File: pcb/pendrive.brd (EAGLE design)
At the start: 100 x 80 mm, 22 parts, among them IC1 MCP1703CB, U1 F55[0/1]X---RGZ48, U2 MICROSD-MOLEX, X1 USBPCB, Y1 RESONATORSMD

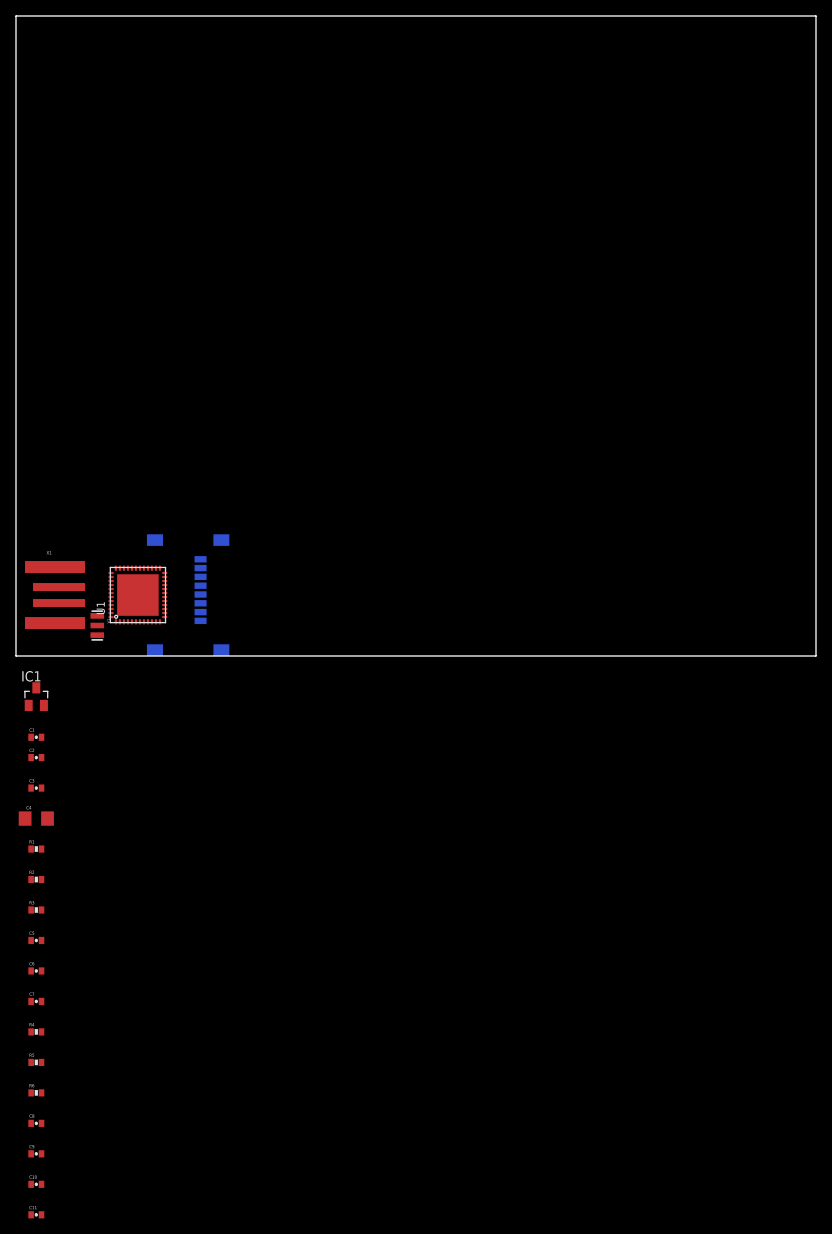
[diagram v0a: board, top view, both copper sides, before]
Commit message: First layout of components, not routed yet
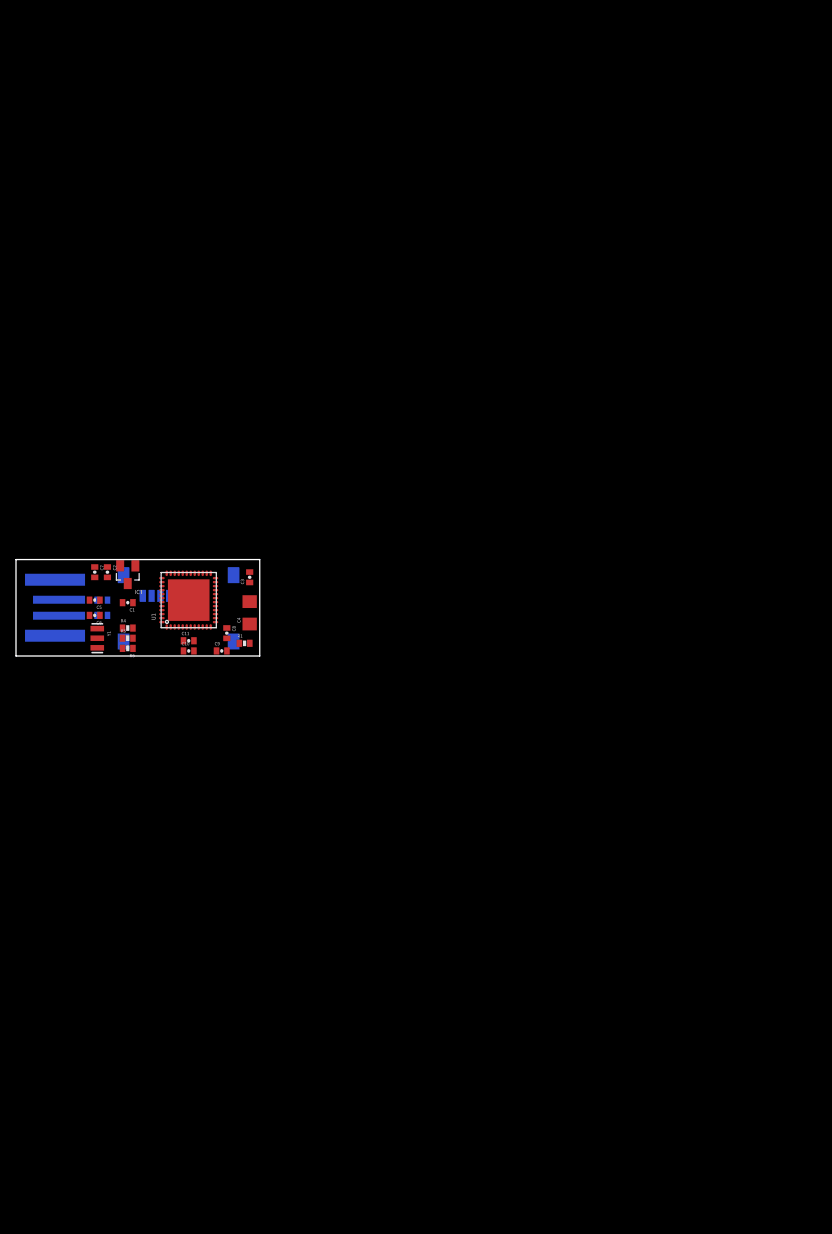
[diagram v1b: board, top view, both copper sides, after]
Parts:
- moved C11 74.2 mm to (21.6, 1.91)
- moved C10 69.3 mm to (21.6, 0.64)
- moved C9 67.0 mm to (25.7, 0.64)
- moved C8 65.7 mm to (26.4, 2.86), turned to 270 degrees
- moved R6 56.7 mm to (14.0, 0.95), turned to 180 degrees
- moved R5 54.2 mm to (14.0, 2.22)
- moved C7 54.2 mm to (9.84, 10.5), turned to 270 degrees
- moved R4 51.8 mm to (14.0, 3.49)
- moved C6 45.0 mm to (9.84, 5.08), turned to 180 degrees
- moved C5 43.2 mm to (9.84, 6.99), turned to 180 degrees
- moved R3 39.6 mm to (10.8, 6.99), flipped to the bottom, turned to 180 degrees
- moved C3 37.5 mm to (29.2, 9.84), turned to 90 degrees
- moved C4 37.0 mm to (29.2, 5.40), turned to 90 degrees
- moved R1 36.6 mm to (28.6, 1.59)
- moved R2 34.0 mm to (10.8, 5.08), flipped to the bottom, turned to 180 degrees
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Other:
- board size 100 x 80 mm -> 30.5 x 12.1 mm

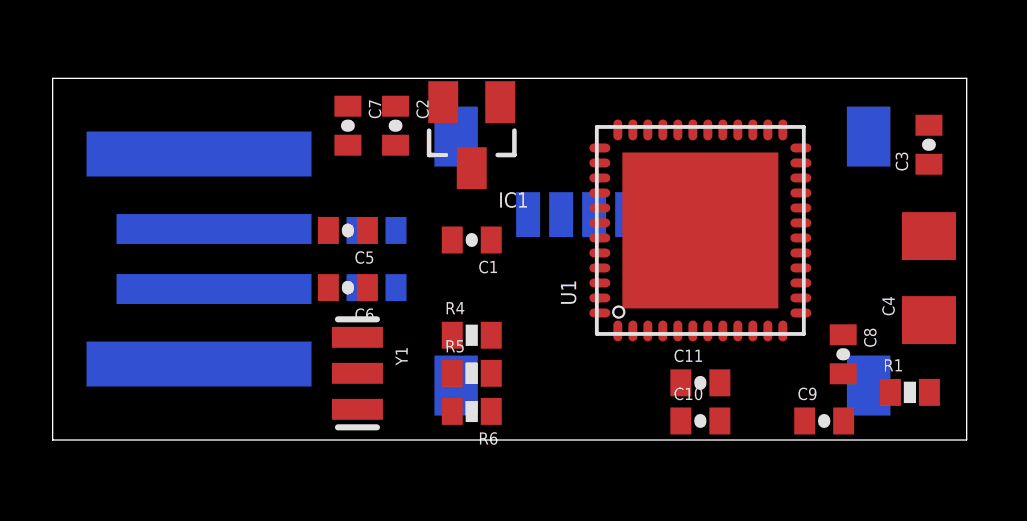
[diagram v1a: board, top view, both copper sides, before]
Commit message: Added first routed PCB version, not tested yet
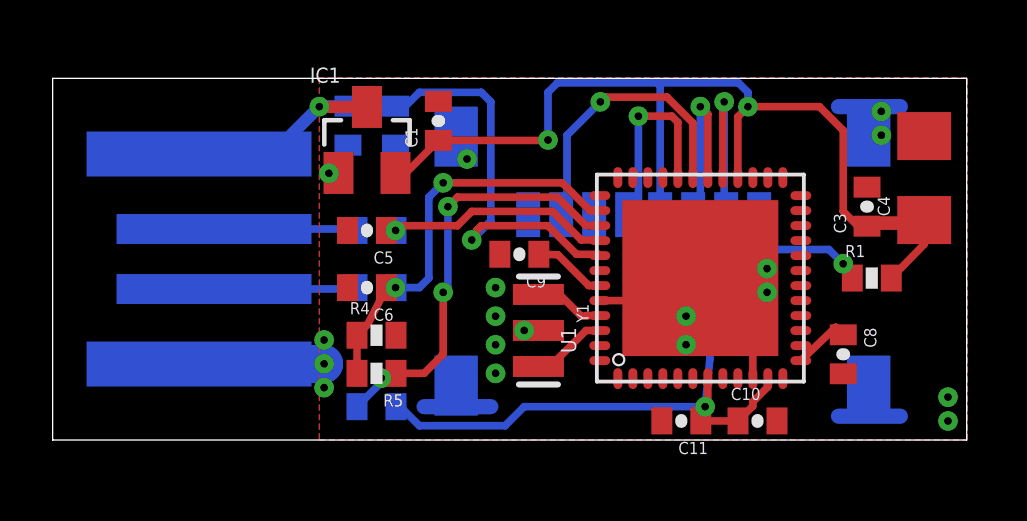
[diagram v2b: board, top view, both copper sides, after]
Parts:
- moved C9 11.6 mm to (15.6, 6.19), turned to 180 degrees
- moved Y1 6.20 mm to (16.2, 3.65)
- moved C1 4.12 mm to (12.9, 10.6), turned to 90 degrees
- moved R1 4.02 mm to (27.3, 5.40)
- moved IC1 3.50 mm to (10.5, 10.0), turned to 0 degrees
- moved C4 3.34 mm to (29.1, 8.73)
- moved R6 3.18 mm to (10.8, 1.11), flipped to the bottom, turned to 0 degrees
- moved R4 3.18 mm to (10.8, 3.49)
- moved R5 3.18 mm to (10.8, 2.22), turned to 180 degrees
- moved C3 2.92 mm to (27.1, 7.78)
- moved C10 1.91 mm to (23.5, 0.64)
- moved U1 1.59 mm to (21.6, 5.40)
- moved C11 1.42 mm to (21.0, 0.64), turned to 180 degrees
- moved C5 0.63 mm to (10.5, 6.99)
- moved C6 0.63 mm to (10.5, 5.08)
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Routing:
- net 3.3V: track 0.00 -> 57.5 mm, vias 0 -> 3
- net 5V: track 0.00 -> 22.2 mm, vias 0 -> 2
- net GND: track 0.00 -> 20.4 mm, vias 0 -> 18
- net PUR: track 0.00 -> 14.3 mm, vias 0 -> 3
- net USB_DP: track 0.00 -> 13.7 mm, vias 0 -> 2
- net SD_CS: track 0.00 -> 12.0 mm, vias 0 -> 2
- net SOMI: track 0.00 -> 9.63 mm, vias 0 -> 1
- net USB_DM: track 0.00 -> 7.81 mm, vias 0 -> 1
- net CLK: track 0.00 -> 6.68 mm, vias 0 -> 1
- net SIMO: track 0.00 -> 6.17 mm, vias 0 -> 1
- net N$2: track 0.00 -> 4.78 mm
- net N$1: track 0.00 -> 4.78 mm
- net N$5: track 0.00 -> 2.55 mm
- net 1.8V: track 0.00 -> 2.46 mm
- net N$4: track 0.00 -> 2.41 mm
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- added copper zone on layer 1, net GND
- added copper zone on layer 16, net GND

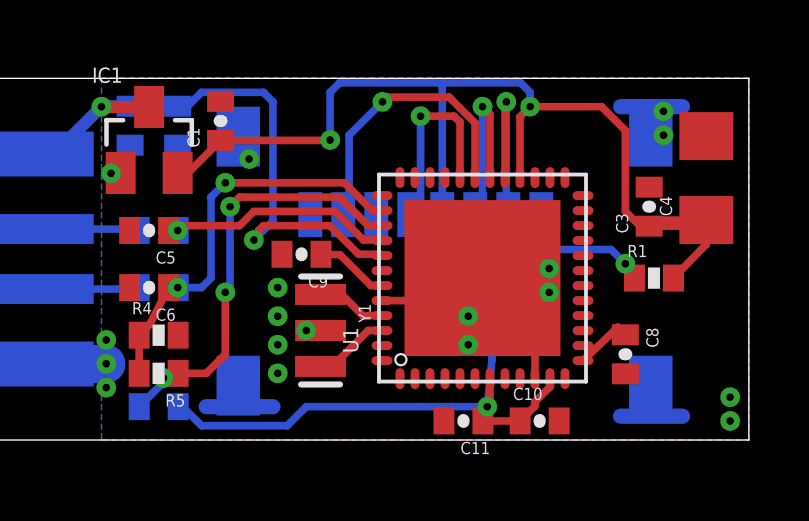
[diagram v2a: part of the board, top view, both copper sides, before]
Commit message: Added programming and test points
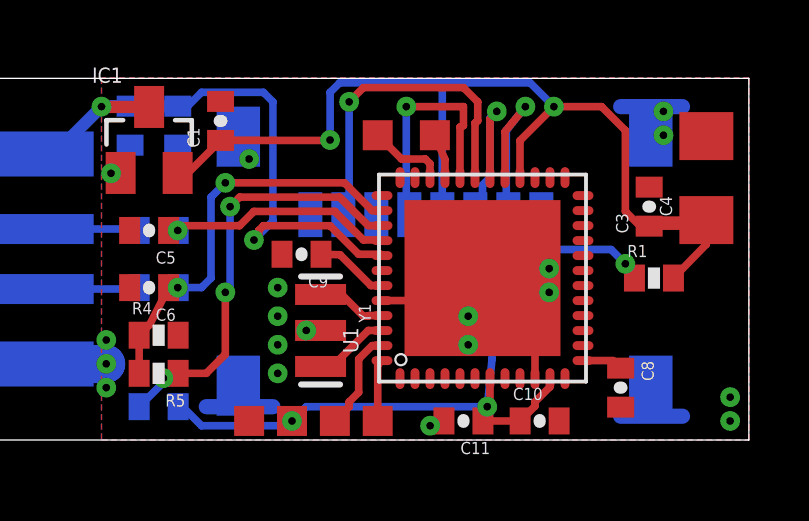
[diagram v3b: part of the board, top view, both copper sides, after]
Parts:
- added TP1, TP2, TP3, TP4, TP5, TP6: PTR1TP10SQ, testpad:TP10SQ
- moved C8 1.12 mm to (26.2, 1.75)
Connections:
- net 3.3V: now also TP3.TP
- net DEBUG_RXD: now also TP5.TP
- net DEBUG_TXD: now also TP6.TP
- net GND: now also TP4.TP
- net RST: now also TP1.TP
- net TEST: now also TP2.TP
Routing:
- net TEST: track 0.00 -> 3.36 mm
- net DEBUG_RXD: track 0.00 -> 2.60 mm
- net RST: track 0.00 -> 2.07 mm
- net DEBUG_TXD: track 0.00 -> 1.48 mm
- net SOMI: track 9.63 -> 11.1 mm
- net CLK: track 6.68 -> 7.96 mm
- net GND: track 20.4 -> 21.5 mm, vias 18 -> 19
- net VCORE: track 1.96 -> 1.36 mm
- net 3.3V: track 57.5 -> 57.6 mm, vias 3 -> 4

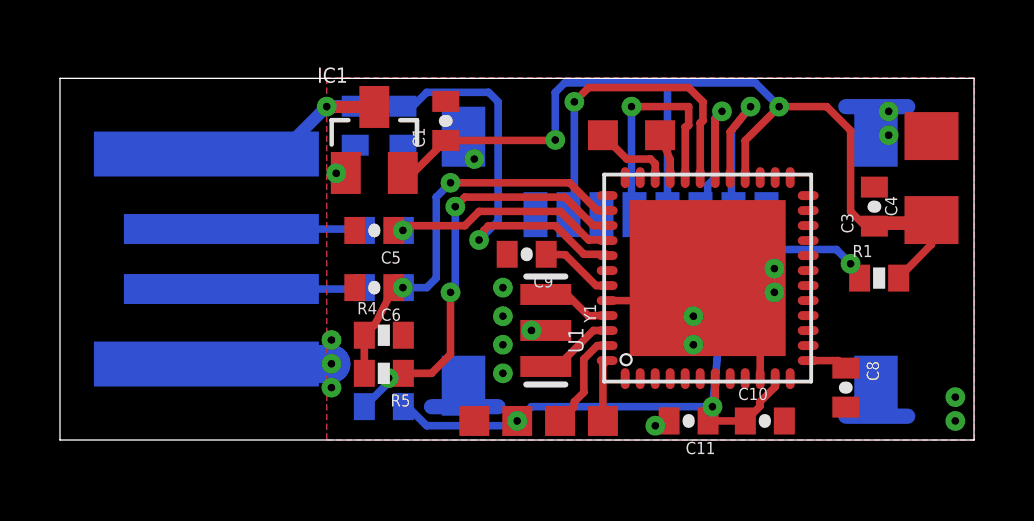
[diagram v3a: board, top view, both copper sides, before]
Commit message: Shrinked the board a little bit
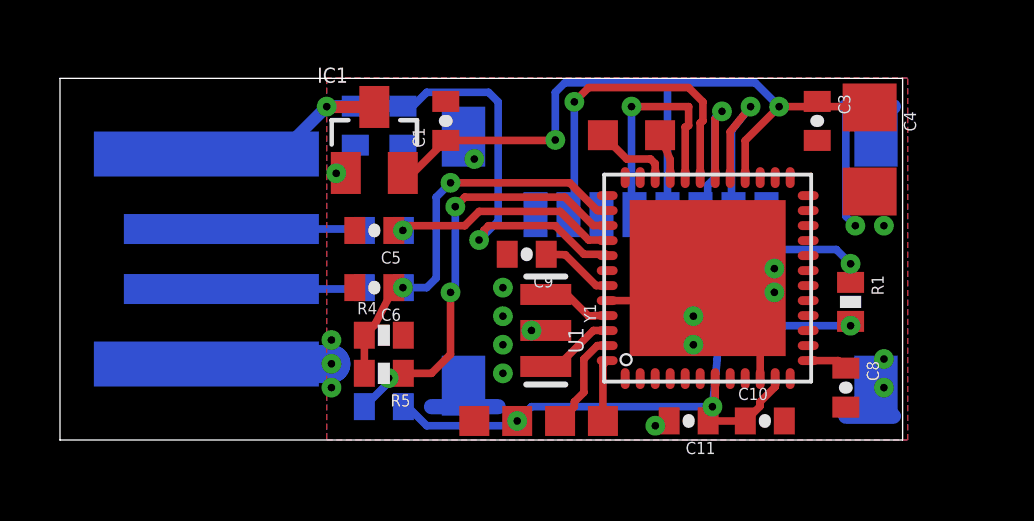
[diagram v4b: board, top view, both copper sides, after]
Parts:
- moved C3 3.43 mm to (25.2, 10.6), turned to 270 degrees
- moved C4 2.27 mm to (27.0, 9.68), turned to 270 degrees
- moved R1 1.24 mm to (26.4, 4.60), turned to 270 degrees
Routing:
- net 3.3V: track 57.6 -> 52.7 mm, vias 4 -> 5
- net GND: track 21.5 -> 25.6 mm
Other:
- board size 30.5 x 12.1 mm -> 28.1 x 12.1 mm
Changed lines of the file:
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@@
 <board>
 <plain>
-<wire x1="0" y1="0" x2="30.4675" y2="0" width="0" layer="20"/>
-<wire x1="30.4675" y1="0" x2="30.4675" y2="12.055" width="0" layer="20"/>
-<wire x1="30.4675" y1="12.055" x2="0" y2="12.055" width="0" layer="20"/>
+<wire x1="0" y1="0" x2="28.08625" y2="0" width="0" layer="20"/>
+<wire x1="28.08625" y1="0" x2="28.08625" y2="12.055" width="0" layer="20"/>
+<wire x1="28.08625" y1="12.055" x2="0" y2="12.055" width="0" layer="20"/>
 <wire x1="0" y1="12.055" x2="0" y2="0" width="0" layer="20"/>
 </plain>
@@
 <element name="C1" library="SparkFun" package="0402-CAP" value="1uF / 10V" x="12.85875" y="10.63625" rot="R90"/>
 <element name="C2" library="SparkFun" package="0402-CAP" value="1uF / 10V" x="11.43" y="10.4775" rot="MR270"/>
-<element name="C3" library="SparkFun" package="0402-CAP" value="0.1uF / 10V" x="27.14625" y="7.77875" rot="R90"/>
-<element name="C4" library="SparkFun" package="1206" value="10uF / 10V" x="29.05125" y="8.73125" rot="R90"/>
-<element name="R1" library="SparkFun" package="0402-RES" value="47k" x="27.305" y="5.3975"/>
+<element name="C3" library="SparkFun" package="0402-CAP" value="0.1uF / 10V" x="25.24125" y="10.63625" rot="R270"/>
+<element name="C4" library="SparkFun" package="1206" value="10uF / 10V" x="26.9875" y="9.68375" rot="R270"/>
+<element name="R1" library="SparkFun" package="0402-RES" value="47k" x="26.3525" y="4.60375" rot="R270"/>
 <element name="R2" library="SparkFun" package="0402-RES" value="27" x="10.795" y="5.08" rot="MR180"/>
 <element name="R3" library="SparkFun" package="0402-RES" value="27" x="10.795" y="6.985" rot="MR180"/>
@@
 <vertex x="8.89" y="12.065"/>
 <vertex x="8.89" y="0"/>
-<vertex x="30.48" y="0"/>
-<vertex x="30.48" y="12.065"/>
+<vertex x="28.2575" y="0"/>
+<vertex x="28.2575" y="12.065"/>
 </polygon>
 <polygon width="0.254" layer="1">
 <vertex x="8.89" y="12.065"/>
 <vertex x="8.89" y="0"/>
-<vertex x="30.48" y="0"/>
-<vertex x="30.48" y="12.065"/>
+<vertex x="28.2575" y="0"/>
+<vertex x="28.2575" y="12.065"/>
 </polygon>
 <via x="9.04875" y="3.33375" extent="1-16" drill="0.254"/>
@@
 <wire x1="12.3825" y1="1.11125" x2="14.605" y2="1.11125" width="0.508" layer="16"/>
 <via x="13.81125" y="9.36625" extent="1-16" drill="0.254"/>
-<wire x1="26.19375" y1="11.1125" x2="28.2575" y2="11.1125" width="0.508" layer="16"/>
-<wire x1="26.19375" y1="0.79375" x2="28.2575" y2="0.79375" width="0.508" layer="16"/>
-<via x="29.845" y="0.635" extent="1-16" drill="0.254"/>
-<via x="29.845" y="1.42875" extent="1-16" drill="0.254"/>
+<wire x1="26.19375" y1="11.1125" x2="27.78125" y2="11.1125" width="0.508" layer="16"/>
+<wire x1="26.19375" y1="0.79375" x2="27.78125" y2="0.79375" width="0.508" layer="16"/>
+<via x="27.46375" y="1.74625" extent="1-16" drill="0.254"/>
+<via x="27.46375" y="2.69875" extent="1-16" drill="0.254"/>
 <via x="21.11375" y="3.175" extent="1-16" drill="0.254"/>
 <via x="21.11375" y="4.1275" extent="1-16" drill="0.254"/>
@@
 <wire x1="18.24" y1="4.6475" x2="20.59375" y2="4.6475" width="0.254" layer="1"/>
 <wire x1="20.59375" y1="4.6475" x2="21.11375" y2="4.1275" width="0.254" layer="1"/>
-<via x="27.6225" y="10.95375" extent="1-16" drill="0.254"/>
-<via x="27.6225" y="10.16" extent="1-16" drill="0.254"/>
+<via x="26.51125" y="7.14375" extent="1-16" drill="0.254"/>
+<via x="27.46375" y="7.14375" extent="1-16" drill="0.254"/>
 <wire x1="4.88" y1="2.5325" x2="9.04125" y2="2.5325" width="1.27" layer="16"/>
 <wire x1="9.04125" y1="2.5325" x2="9.04875" y2="2.54" width="1.27" layer="16"/>
 <via x="9.2075" y="8.89" extent="1-16" drill="0.254"/>
-<wire x1="28.2575" y1="11.1125" x2="27.78125" y2="11.1125" width="0.254" layer="16"/>
-<wire x1="27.78125" y1="11.1125" x2="27.6225" y2="10.95375" width="0.254" layer="16"/>
 <wire x1="23.34" y1="2.0475" x2="23.34" y2="4.44875" width="0.254" layer="1"/>
 <wire x1="23.34" y1="4.44875" x2="23.8125" y2="4.92125" width="0.254" layer="1"/>
@@
 <wire x1="19.84375" y1="0.47625" x2="20.16125" y2="0.635" width="0.254" layer="16"/>
 <wire x1="20.16125" y1="0.635" x2="20.32" y2="0.47625" width="0.254" layer="16"/>
+<wire x1="26.19375" y1="11.1125" x2="26.19375" y2="7.46125" width="0.254" layer="16"/>
+<wire x1="26.19375" y1="7.46125" x2="26.51125" y2="7.14375" width="0.254" layer="16"/>
+<wire x1="26.19375" y1="0.79375" x2="26.51125" y2="0.79375" width="0.254" layer="16"/>
+<wire x1="26.51125" y1="0.79375" x2="27.46375" y2="1.74625" width="0.254" layer="16"/>
 </signal>
 <signal name="N$4">
@@
 <wire x1="20.25" y1="7.5125" x2="20.25" y2="6.1025" width="0.254" layer="16"/>
 <wire x1="20.25" y1="6.1025" x2="21.9075" y2="4.445" width="0.254" layer="16"/>
-<wire x1="21.9075" y1="4.445" x2="21.9075" y2="2.69875" width="0.254" layer="16"/>
+<wire x1="21.9075" y1="4.445" x2="21.9075" y2="3.81" width="0.254" layer="16"/>
+<wire x1="21.9075" y1="3.81" x2="21.9075" y2="2.69875" width="0.254" layer="16"/>
 <wire x1="21.9075" y1="2.69875" x2="21.74875" y2="1.11125" width="0.254" layer="16"/>
 <via x="21.74875" y="1.11125" extent="1-16" drill="0.254"/>
@@
 <wire x1="21.605" y1="1.11125" x2="21.605" y2="1.12625" width="0.254" layer="16"/>
 <wire x1="21.605" y1="1.12625" x2="21.74875" y2="1.11125" width="0.254" layer="16"/>
-<wire x1="27.14625" y1="7.12875" x2="28.84875" y2="7.12875" width="0.254" layer="1"/>
-<wire x1="28.84875" y1="7.12875" x2="29.05125" y2="7.33125" width="0.254" layer="1"/>
-<wire x1="29.05125" y1="7.33125" x2="29.05125" y2="6.52375" width="0.254" layer="1"/>
-<wire x1="29.05125" y1="6.52375" x2="27.955" y2="5.3975" width="0.254" layer="1"/>
-<wire x1="29.05125" y1="7.33125" x2="27.01625" y2="7.33125" width="0.254" layer="1"/>
-<wire x1="27.01625" y1="7.33125" x2="26.82875" y2="7.14375" width="0.254" layer="1"/>
-<wire x1="26.82875" y1="7.14375" x2="26.3525" y2="7.62" width="0.254" layer="1"/>
-<wire x1="26.3525" y1="7.62" x2="26.3525" y2="10.31875" width="0.254" layer="1"/>
-<wire x1="26.3525" y1="10.31875" x2="25.55875" y2="11.1125" width="0.254" layer="1"/>
 <wire x1="21.84" y1="2.0475" x2="21.84" y2="1.2025" width="0.254" layer="1"/>
 <wire x1="21.84" y1="1.2025" x2="21.74875" y2="1.11125" width="0.254" layer="1"/>
@@
 <wire x1="22.84" y1="8.7475" x2="22.84" y2="9.98125" width="0.254" layer="1"/>
 <wire x1="22.84" y1="9.98125" x2="23.97125" y2="11.1125" width="0.254" layer="1"/>
-<wire x1="25.55875" y1="11.1125" x2="23.97125" y2="11.1125" width="0.254" layer="1"/>
 <wire x1="23.1775" y1="11.90625" x2="23.97125" y2="11.1125" width="0.254" layer="16"/>
+<wire x1="23.97125" y1="11.1125" x2="25.385" y2="11.1125" width="0.254" layer="1"/>
+<wire x1="25.385" y1="11.1125" x2="25.24125" y2="11.28625" width="0.254" layer="1"/>
+<wire x1="25.385" y1="11.1125" x2="26.95875" y2="11.1125" width="0.254" layer="1"/>
+<wire x1="26.95875" y1="11.1125" x2="26.9875" y2="11.08375" width="0.254" layer="1"/>
+<wire x1="26.3525" y1="3.95375" x2="26.3525" y2="3.81" width="0.254" layer="1"/>
+<via x="26.3525" y="3.81" extent="1-16" drill="0.254"/>
+<wire x1="26.3525" y1="3.81" x2="21.9075" y2="3.81" width="0.254" layer="16"/>
 </signal>
 <signal name="CLK">
@@
 <wire x1="25.87625" y1="6.35" x2="26.3525" y2="5.87375" width="0.254" layer="16"/>
 <via x="26.3525" y="5.87375" extent="1-16" drill="0.254"/>
-<wire x1="26.3525" y1="5.87375" x2="26.3525" y2="5.7" width="0.254" layer="1"/>
-<wire x1="26.3525" y1="5.7" x2="26.655" y2="5.3975" width="0.254" layer="1"/>
+<wire x1="26.3525" y1="5.87375" x2="26.3525" y2="5.25375" width="0.254" layer="1"/>
 <wire x1="22.34" y1="8.7475" x2="22.34" y2="10.275" width="0.254" layer="1"/>
 <wire x1="22.34" y1="10.275" x2="23.01875" y2="11.1125" width="0.254" layer="1"/>
